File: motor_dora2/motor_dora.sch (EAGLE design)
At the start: 38 parts

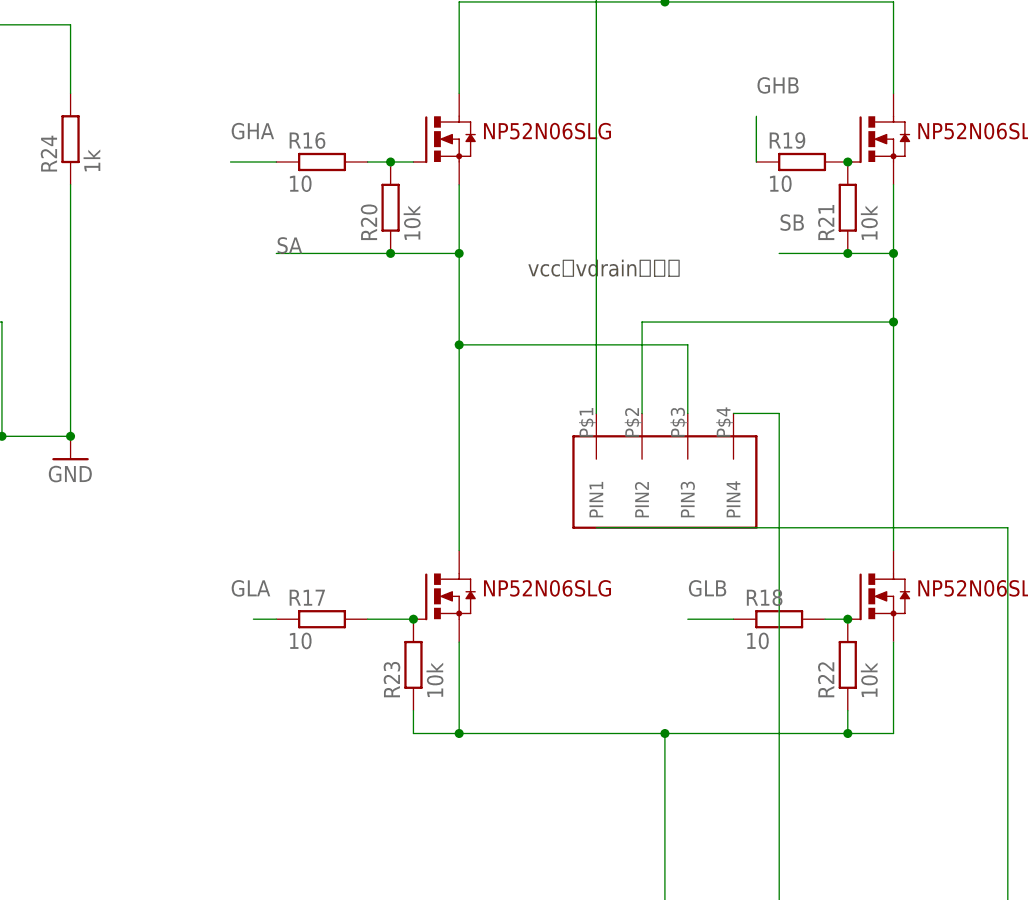
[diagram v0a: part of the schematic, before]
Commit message: ゲート駆動を調整
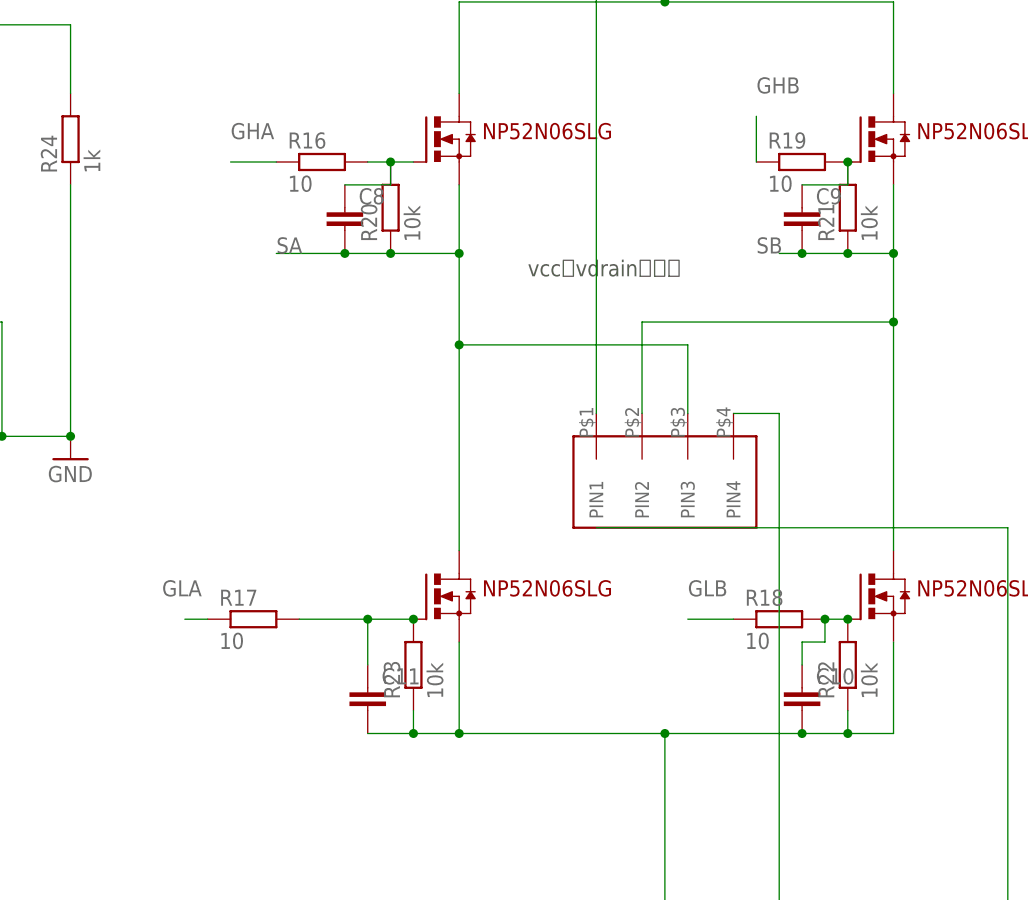
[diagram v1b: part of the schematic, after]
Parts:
- added C10, C11, C8, C9: (no value), rcl:C-EUC2012
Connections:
- net GND: now also C10.2, C11.2
- net N$24: now also C8.1
- net N$25: now also C9.1
- net N$26: now also C11.1
- net N$27: now also C10.1
- net SA: now also C8.2
- net SB: now also C9.2
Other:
- moved on the sheet: R17
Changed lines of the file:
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@@
 <part name="U$5" library="user" deviceset="1005X4RESISTOR" device="" value="10k"/>
 <part name="U$6" library="user" deviceset="1005X4RESISTOR" device="" value="10k"/>
+<part name="C8" library="rcl" library_urn="urn:adsk.eagle:library:334" deviceset="C-EU" device="C2012" package3d_urn="urn:adsk.eagle:package:23625/2"/>
+<part name="C9" library="rcl" library_urn="urn:adsk.eagle:library:334" deviceset="C-EU" device="C2012" package3d_urn="urn:adsk.eagle:package:23625/2"/>
+<part name="C10" library="rcl" library_urn="urn:adsk.eagle:library:334" deviceset="C-EU" device="C2012" package3d_urn="urn:adsk.eagle:package:23625/2"/>
+<part name="C11" library="rcl" library_urn="urn:adsk.eagle:library:334" deviceset="C-EU" device="C2012" package3d_urn="urn:adsk.eagle:package:23625/2"/>
 </parts>
 <sheets>
@@
 <attribute name="VALUE" x="250.19" y="80.518" size="1.778" layer="96"/>
 </instance>
-<instance part="R17" gate="G$1" x="254" y="33.02" smashed="yes">
-<attribute name="NAME" x="250.19" y="34.5186" size="1.778" layer="95"/>
-<attribute name="VALUE" x="250.19" y="29.718" size="1.778" layer="96"/>
+<instance part="R17" gate="G$1" x="246.38" y="33.02" smashed="yes">
+<attribute name="NAME" x="242.57" y="34.5186" size="1.778" layer="95"/>
+<attribute name="VALUE" x="242.57" y="29.718" size="1.778" layer="96"/>
 </instance>
 <instance part="R18" gate="G$1" x="304.8" y="33.02" smashed="yes">
@@
 <instance part="U$5" gate="G$1" x="-53.34" y="53.34" smashed="yes"/>
 <instance part="U$6" gate="G$1" x="165.1" y="91.44" smashed="yes" rot="R90"/>
+<instance part="C8" gate="G$1" x="256.54" y="78.74" smashed="yes">
+<attribute name="NAME" x="258.064" y="79.121" size="1.778" layer="95"/>
+<attribute name="VALUE" x="258.064" y="74.041" size="1.778" layer="96"/>
+</instance>
+<instance part="C9" gate="G$1" x="307.34" y="78.74" smashed="yes">
+<attribute name="NAME" x="308.864" y="79.121" size="1.778" layer="95"/>
+<attribute name="VALUE" x="308.864" y="74.041" size="1.778" layer="96"/>
+</instance>
+<instance part="C10" gate="G$1" x="307.34" y="25.4" smashed="yes">
+<attribute name="NAME" x="308.864" y="25.781" size="1.778" layer="95"/>
+<attribute name="VALUE" x="308.864" y="20.701" size="1.778" layer="96"/>
+</instance>
+<instance part="C11" gate="G$1" x="259.08" y="25.4" smashed="yes">
+<attribute name="NAME" x="260.604" y="25.781" size="1.778" layer="95"/>
+<attribute name="VALUE" x="260.604" y="20.701" size="1.778" layer="96"/>
+</instance>
 </instances>
 <busses>
@@
 <wire x1="269.24" y1="20.32" x2="292.1" y2="20.32" width="0.1524" layer="91"/>
 <pinref part="U$11" gate="G$1" pin="PIN3_S"/>
-<wire x1="292.1" y1="20.32" x2="312.42" y2="20.32" width="0.1524" layer="91"/>
+<wire x1="292.1" y1="20.32" x2="307.34" y2="20.32" width="0.1524" layer="91"/>
+<wire x1="307.34" y1="20.32" x2="312.42" y2="20.32" width="0.1524" layer="91"/>
 <wire x1="312.42" y1="20.32" x2="317.5" y2="20.32" width="0.1524" layer="91"/>
 <wire x1="317.5" y1="20.32" x2="317.5" y2="30.48" width="0.1524" layer="91"/>
@@
 <wire x1="304.8" y1="55.88" x2="304.8" y2="-17.78" width="0.1524" layer="91"/>
 <junction x="304.8" y="-17.78"/>
+<pinref part="C10" gate="G$1" pin="2"/>
+<junction x="307.34" y="20.32"/>
+<pinref part="C11" gate="G$1" pin="2"/>
+<wire x1="259.08" y1="20.32" x2="264.16" y2="20.32" width="0.1524" layer="91"/>
+<junction x="264.16" y="20.32"/>
 </segment>
 <segment>
@@
 <label x="248.92" y="73.66" size="1.778" layer="95"/>
 <pinref part="R20" gate="G$1" pin="1"/>
-<wire x1="261.62" y1="73.66" x2="248.92" y2="73.66" width="0.1524" layer="91"/>
+<wire x1="261.62" y1="73.66" x2="256.54" y2="73.66" width="0.1524" layer="91"/>
 <junction x="261.62" y="73.66"/>
+<wire x1="256.54" y1="73.66" x2="248.92" y2="73.66" width="0.1524" layer="91"/>
 <wire x1="294.64" y1="63.5" x2="294.64" y2="55.88" width="0.1524" layer="91"/>
 <pinref part="U$14" gate="G$1" pin="PIN3"/>
 <wire x1="294.64" y1="63.5" x2="269.24" y2="63.5" width="0.1524" layer="91"/>
 <junction x="269.24" y="63.5"/>
+<pinref part="C8" gate="G$1" pin="2"/>
+<junction x="256.54" y="73.66"/>
 </segment>
 </net>
@@
 <wire x1="317.5" y1="73.66" x2="312.42" y2="73.66" width="0.1524" layer="91"/>
 <junction x="317.5" y="73.66"/>
-<label x="304.8" y="76.2" size="1.778" layer="95"/>
-<wire x1="312.42" y1="73.66" x2="304.8" y2="73.66" width="0.1524" layer="91"/>
+<label x="302.26" y="73.66" size="1.778" layer="95"/>
+<wire x1="312.42" y1="73.66" x2="307.34" y2="73.66" width="0.1524" layer="91"/>
 <pinref part="R21" gate="G$1" pin="1"/>
 <junction x="312.42" y="73.66"/>
+<wire x1="307.34" y1="73.66" x2="304.8" y2="73.66" width="0.1524" layer="91"/>
 <wire x1="289.56" y1="66.04" x2="289.56" y2="55.88" width="0.1524" layer="91"/>
 <pinref part="U$14" gate="G$1" pin="PIN2"/>
 <wire x1="289.56" y1="66.04" x2="317.5" y2="66.04" width="0.1524" layer="91"/>
 <junction x="317.5" y="66.04"/>
+<pinref part="C9" gate="G$1" pin="2"/>
+<junction x="307.34" y="73.66"/>
 </segment>
 </net>
@@
 <segment>
 <pinref part="R17" gate="G$1" pin="1"/>
-<wire x1="248.92" y1="33.02" x2="246.38" y2="33.02" width="0.1524" layer="91"/>
-<label x="243.84" y="35.56" size="1.778" layer="95"/>
+<wire x1="241.3" y1="33.02" x2="238.76" y2="33.02" width="0.1524" layer="91"/>
+<label x="236.22" y="35.56" size="1.778" layer="95"/>
 </segment>
 </net>
@@
 <wire x1="261.62" y1="83.82" x2="259.08" y2="83.82" width="0.1524" layer="91"/>
 <junction x="261.62" y="83.82"/>
+<pinref part="C8" gate="G$1" pin="1"/>
+<wire x1="256.54" y1="81.28" x2="261.62" y2="81.28" width="0.1524" layer="91"/>
+<wire x1="261.62" y1="81.28" x2="261.62" y2="83.82" width="0.1524" layer="91"/>
 </segment>
 </net>
@@
 <pinref part="R21" gate="G$1" pin="2"/>
 <junction x="312.42" y="83.82"/>
+<pinref part="C9" gate="G$1" pin="1"/>
+<wire x1="307.34" y1="81.28" x2="312.42" y2="81.28" width="0.1524" layer="91"/>
+<wire x1="312.42" y1="81.28" x2="312.42" y2="83.82" width="0.1524" layer="91"/>
 </segment>
 </net>
@@
 <pinref part="R23" gate="G$1" pin="2"/>
 <junction x="264.16" y="33.02"/>
+<pinref part="C11" gate="G$1" pin="1"/>
+<wire x1="259.08" y1="33.02" x2="251.46" y2="33.02" width="0.1524" layer="91"/>
+<wire x1="259.08" y1="27.94" x2="259.08" y2="33.02" width="0.1524" layer="91"/>
+<junction x="259.08" y="33.02"/>
 </segment>
 </net>
@@
 <pinref part="R22" gate="G$1" pin="2"/>
 <junction x="312.42" y="33.02"/>
-</segment>
-</net>
+<pinref part="C10" gate="G$1" pin="1"/>
+<wire x1="307.34" y1="27.94" x2="307.34" y2="30.48" width="0.1524" layer="91"/>
+<wire x1="307.34" y1="30.48" x2="309.88" y2="30.48" width="0.1524" layer="91"/>
+<wire x1="309.88" y1="30.48" x2="309.88" y2="33.02" width="0.1524" layer="91"/>
+<junction x="309.88" y="33.02"/>
+</segment>
+</net>

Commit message: pwm入力をプルダウンにした
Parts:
- removed R14, R15, R24: 1k, rcl:R-EU_R2012
- added R_I1: 1k, user_rcl:R_SHUGOU
- added U$12, U$15, U$19, U$7: SBR10M100P5Q, user_diode:SBR10M100P5Q
- U$10, U$11, U$8, U$9: value NP52N06SLG -> IPD034N06N3G; device user:NP52N06SLG -> user_tr_fet_igbt:IPD034N06N3G
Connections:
- net GND: now also R_I1.3, U$10.PIN3_S, U$12.A1, U$12.A2, U$5.5, U$5.6, U$6.8, U$7.A1, U$7.A2; no longer R24.1, U$6.7, U$9.PIN3_S
- net N$14: now also R_I1.7, U$4.G_K; no longer R24.2, U$4.B_K
- net N$15: now also U$6.3; no longer U$6.4
- net N$18: now also R_I1.2; no longer R14.1
- net N$19: now also R_I1.8, U$4.R_K; no longer R15.1, U$18.PIN6_D1
- net N$20: now also R_I1.6, U$4.B_K; no longer R14.2, U$4.G_K
- net N$21: now also R_I1.1, U$18.PIN6_D1; no longer R15.2, U$4.R_K
- net N$25: now also U$9.PIN1_G; no longer U$10.PIN1_G
- net N$26: now also U$10.PIN1_G; no longer U$9.PIN1_G
- net N$5: now also U$6.4; no longer U$6.3
- net SA: now also U$10.PIN2_D, U$19.A1, U$19.A2, U$7.K; no longer U$9.PIN2_D
- net SB: now also U$12.K, U$15.A1, U$15.A2, U$9.PIN3_S; no longer U$10.PIN3_S
- net V5: now also U$6.7; no longer U$5.5, U$5.6, U$6.8
- net VCC: now also U$15.K, U$19.K, U$9.PIN2_D; no longer U$10.PIN2_D
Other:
- moved on the sheet: C10, C11, C8, C9
